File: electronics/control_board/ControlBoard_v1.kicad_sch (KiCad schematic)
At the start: 27 parts, among them J1 Motor1, J2 Motor2, J3 Motor3, J4 Encoder, J5 I2C, J7 Power, U1 ROB-14450, U2 ROB-14450, U3 ROB-14450, U4 DCDC_Converter

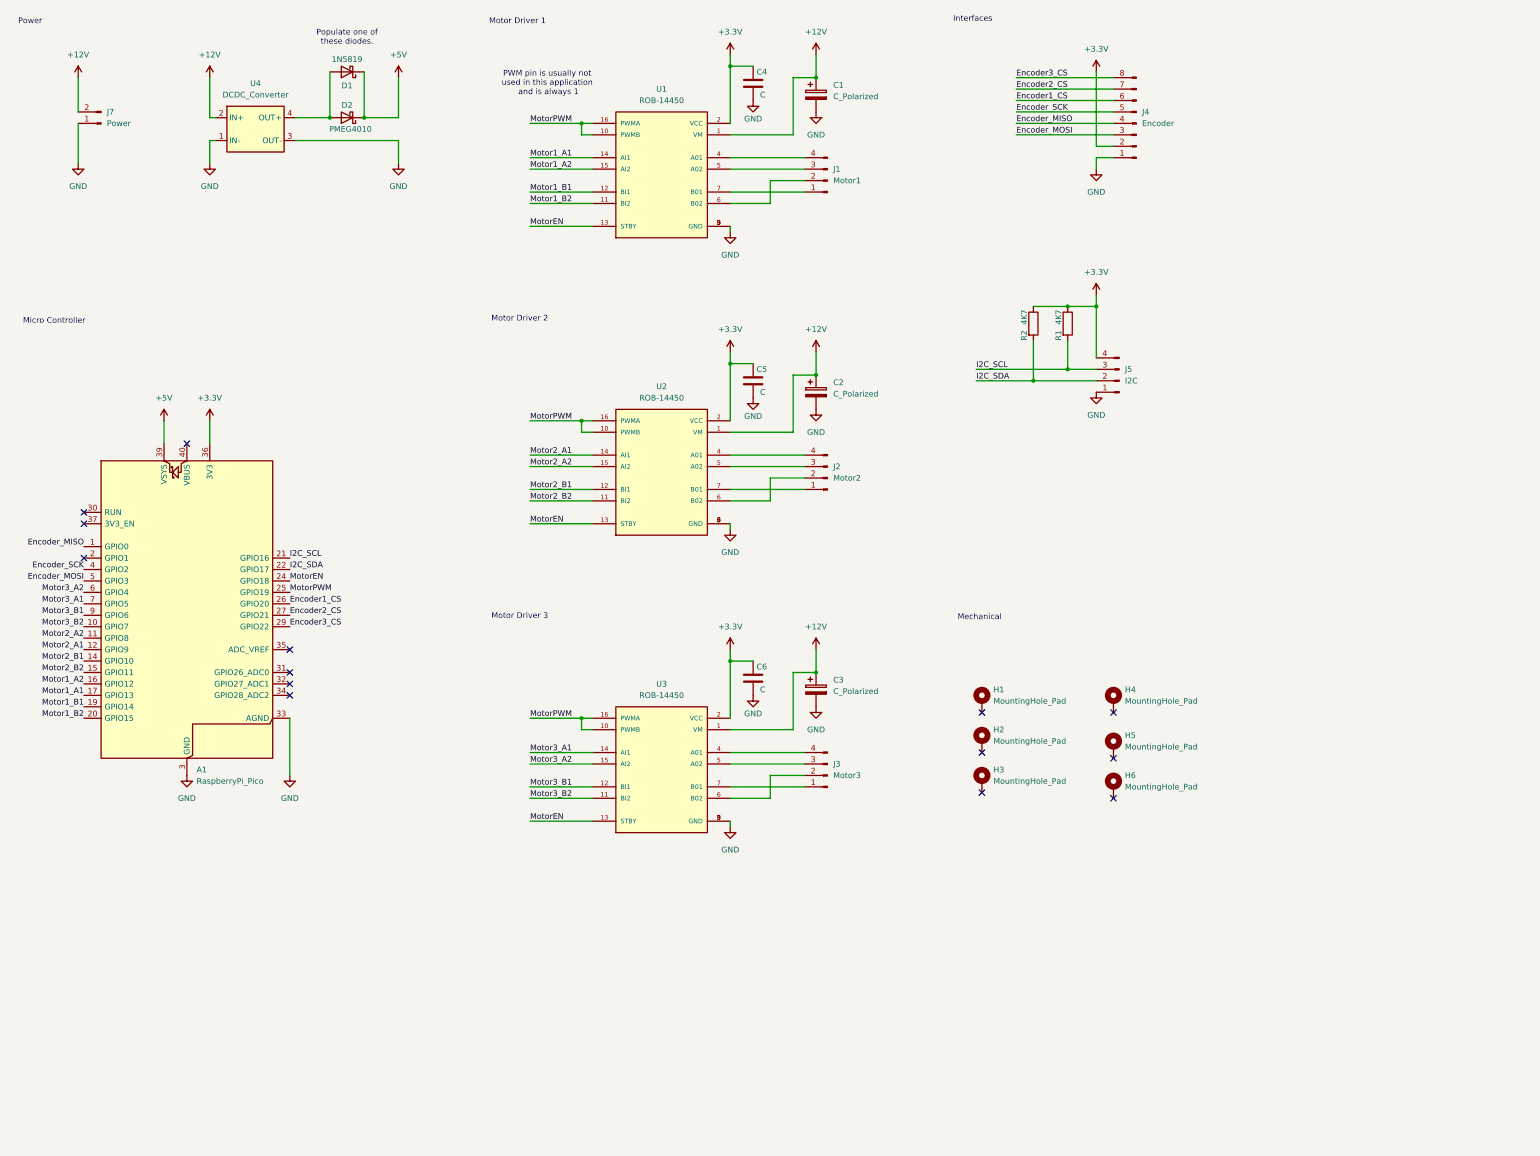
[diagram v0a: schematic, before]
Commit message: Worked on PCB (moved to 4 layers)
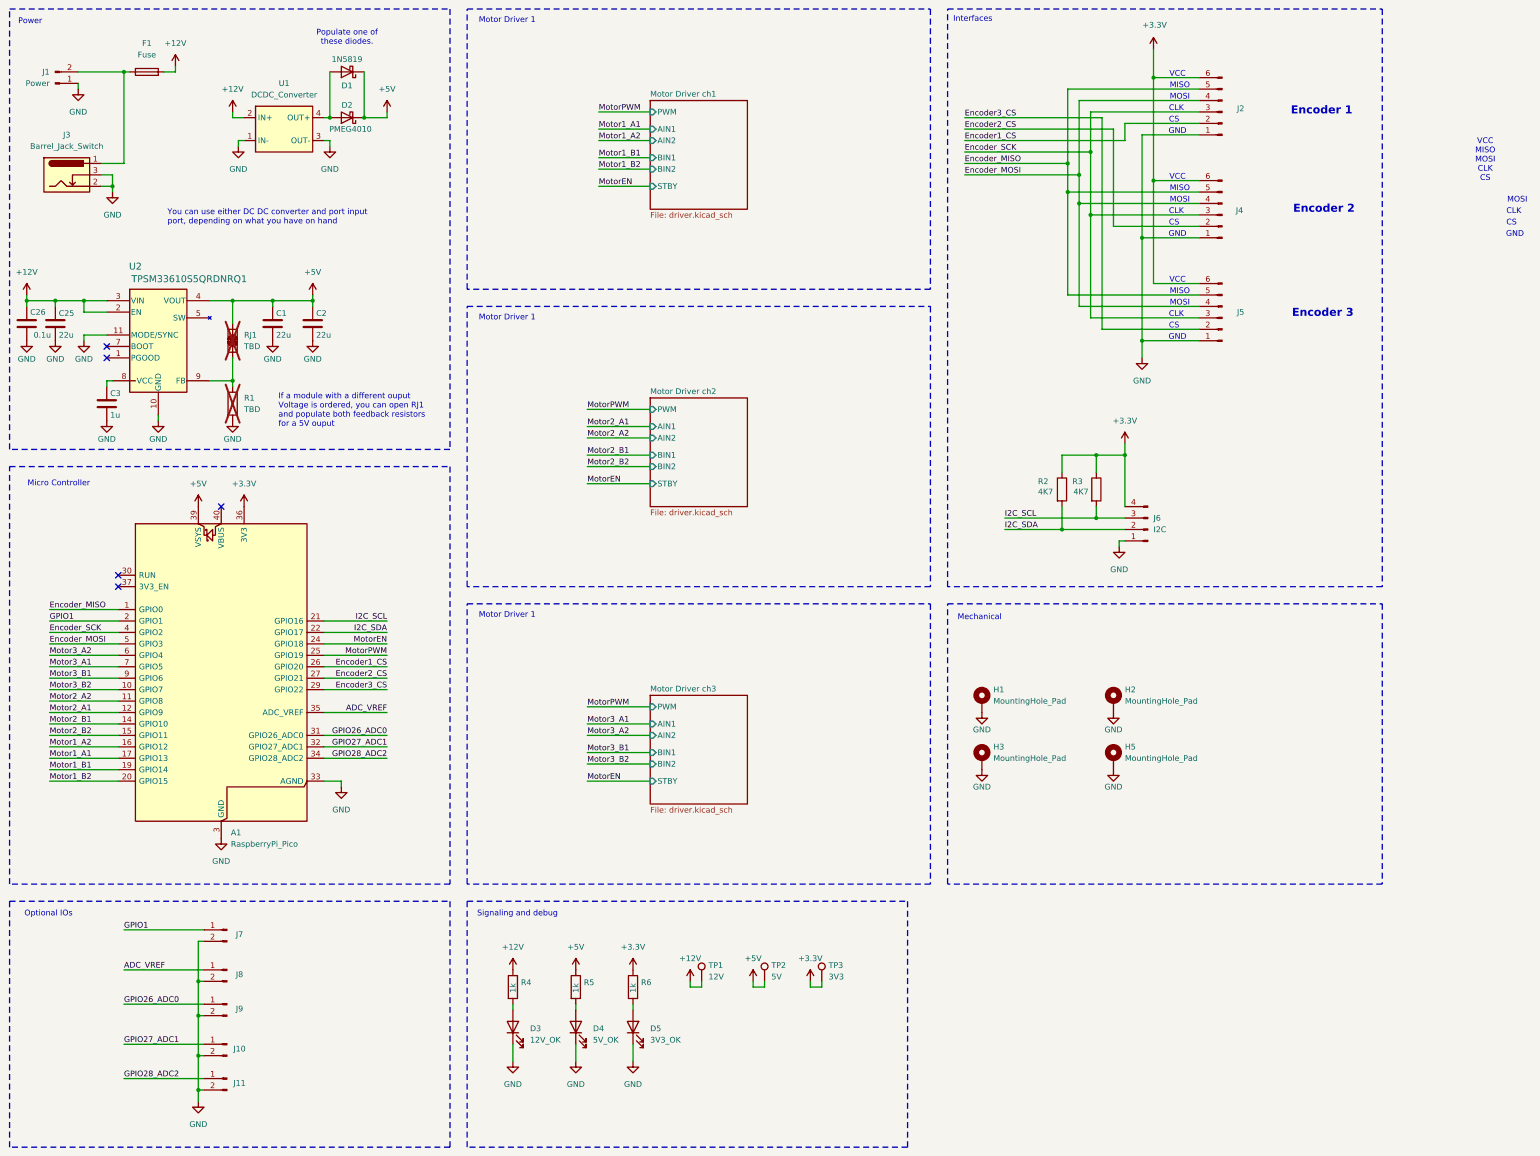
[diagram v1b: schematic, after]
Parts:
- removed C1, C2, C3: C_Polarized, Capacitor_THT:CP_Radial_D8.0mm_P3.50mm, symbol Device:C_Polarized
- removed C4, C5, C6: C, Capacitor_SMD:C_0603_1608Metric_Pad1.08x0.95mm_HandSolder, symbol Device:C
- removed H5, H6: MountingHole_Pad, MountingHole:MountingHole_2.7mm_M2.5_Pad_Via, symbol Mechanical:MountingHole_Pad
- removed J1: Motor1, Connector_PinHeader_2.54mm:PinHeader_1x04_P2.54mm_Vertical, symbol Connector:Conn_01x04_Pin
- removed J2: Motor2, Connector_PinHeader_2.54mm:PinHeader_1x04_P2.54mm_Vertical, symbol Connector:Conn_01x04_Pin
- removed J3: Motor3, Connector_PinHeader_2.54mm:PinHeader_1x04_P2.54mm_Vertical, symbol Connector:Conn_01x04_Pin
- removed J4: Encoder, Connector_JST:JST_PH_B8B-PH-K_1x08_P2.00mm_Vertical, symbol Connector:Conn_01x08_Pin
- removed U1, U2, U3: ROB-14450, ROB-14450:MODULE_ROB-14450, symbol ROB-14450:ROB-14450
- added C1, C2, C25: 22u, Capacitor_SMD:C_0805_2012Metric_Pad1.18x1.45mm_HandSolder, symbol Device:C
- added C26: 0.1u, Capacitor_SMD:C_0603_1608Metric_Pad1.08x0.95mm_HandSolder, symbol Device:C
- added C3: 1u, Capacitor_SMD:C_0805_2012Metric_Pad1.18x1.45mm_HandSolder, symbol Device:C
- added D3: 12V_OK, LED_SMD:LED_0805_2012Metric_Pad1.15x1.40mm_HandSolder, symbol Device:LED
- added D4: 5V_OK, LED_SMD:LED_0805_2012Metric_Pad1.15x1.40mm_HandSolder, symbol Device:LED
- added D5: 3V3_OK, LED_SMD:LED_0805_2012Metric_Pad1.15x1.40mm_HandSolder, symbol Device:LED
- added F1: Fuse, Fuse:Fuse_1206_3216Metric_Pad1.42x1.75mm_HandSolder, symbol Device:Fuse
- added J10, J11, J7, J8, J9: Conn_01x02_Pin, Connector_PinHeader_2.54mm:PinHeader_1x02_P2.54mm_Vertical, symbol Connector:Conn_01x02_Pin
- added J2, J4, J5: Conn_01x06_Pin, Connector_JST:JST_PH_B6B-PH-K_1x06_P2.00mm_Vertical, symbol Connector:Conn_01x06_Pin
- added J3: Barrel_Jack_Switch, Connector_BarrelJack:BarrelJack_Horizontal, symbol Connector:Barrel_Jack_Switch
- added R1: TBD, Resistor_SMD:R_0603_1608Metric_Pad0.98x0.95mm_HandSolder, symbol Device:R
- added R4, R5, R6: 1k, Resistor_SMD:R_0603_1608Metric_Pad0.98x0.95mm_HandSolder, symbol Device:R
- added RJ1: TBD, Additions:0603_shorted_resistor, symbol additions:R_Optional
- added TP1: 12V, TestPoint:TestPoint_Pad_D2.0mm, symbol Connector:TestPoint
- added TP2: 5V, TestPoint:TestPoint_Pad_D2.0mm, symbol Connector:TestPoint
- added TP3: 3V3, TestPoint:TestPoint_Pad_D2.0mm, symbol Connector:TestPoint
- added U2: TPSM33610S5QRDNRQ1, Additions:TPSM33610S5QRDNRQ1, symbol additions:TPSM33610S3QRDNRQ1
- A1: Distributor (none) -> Digikey; Distributor Number (none) -> 2648-SC0918CT-ND
- D1: Distributor (none) -> Digikey; Distributor Number (none) -> 1801-1N5819CT-ND
- D2: Distributor (none) -> Digikey; Distributor Number (none) -> -
- H1: Distributor (none) -> -; Distributor Number (none) -> -
- H2: renamed from H4; Distributor (none) -> -; Distributor Number (none) -> -
- H3: renamed from H2; Distributor (none) -> -; Distributor Number (none) -> -
- H5: renamed from H3; Distributor (none) -> -; Distributor Number (none) -> -
- J1: renamed from J7; Distributor (none) -> Digikey; Distributor Number (none) -> 1738-1437-ND
- J6: renamed from J5; Distributor (none) -> Digikey; Distributor Number (none) -> 455-B4B-XH-A-ND
- R2: Distributor (none) -> Digikey; Distributor Number (none) -> 541-4.70KHCT-ND
- R3: renamed from R1; Distributor (none) -> Digikey; Distributor Number (none) -> 541-4.70KHCT-ND
- U1: renamed from U4; Distributor (none) -> ?; Distributor Number (none) -> -
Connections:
- net +12V: now also C25.1, C26.1, F1.2, R4.1, TP1.1, U2.2 (EN), U2.3 (VIN); no longer J1.2 (Pin_2)
- net +3.3V: now also J2.6 (Pin_6), J4.6 (Pin_6), J5.6 (Pin_6), R6.1, TP3.1
- net +5V: now also C1.1, C2.1, R5.1, RJ1.1, TP2.1, U2.4 (VOUT)
- net Encoder1_CS: now also J2.2 (Pin_2)
- net Encoder2_CS: now also J4.2 (Pin_2)
- net Encoder3_CS: now also J5.2 (Pin_2)
- net Encoder_MISO: now also J2.5 (Pin_5), J4.5 (Pin_5), J5.5 (Pin_5)
- net Encoder_MOSI: now also J2.4 (Pin_4), J4.4 (Pin_4), J5.4 (Pin_4)
- net Encoder_SCK: now also J2.3 (Pin_3), J4.3 (Pin_3), J5.3 (Pin_3)
- net GND: now also H1.1, H2.1, H3.1, H5.1, C1.2, C2.2, C25.2, C26.2, C3.2, D3.1 (K), D4.1 (K), D5.1 (K), J10.2 (Pin_2), J11.2 (Pin_2), J2.1 (Pin_1), J3.2, J3.3, J4.1 (Pin_1), J5.1 (Pin_1), J7.2 (Pin_2), J8.2 (Pin_2), J9.2 (Pin_2), R1.2, U2.10 (GND), U2.11 (MODE/SYNC)
- net GPIO1: now reaches A1.2 (GPIO1)
- net GPIO1: now also J7.1 (Pin_1)
- net GPIO26_ADC0: now reaches A1.31 (GPIO26_ADC0)
- net GPIO26_ADC0: now also J9.1 (Pin_1)
- net GPIO27_ADC1: now reaches A1.32 (GPIO27_ADC1)
- net GPIO27_ADC1: now also J10.1 (Pin_1)
- net GPIO28_ADC2: now reaches A1.34 (GPIO28_ADC2)
- net GPIO28_ADC2: now also J11.1 (Pin_1)
- net ADC_VREF: now reaches A1.35 (ADC_VREF)
- net ADC_VREF: now also J8.1 (Pin_1)
- new net: D5.2 (A), R6.2
- new net: R1.1, RJ1.2, U2.9 (FB)
- new net: F1.1, J1.2 (Pin_2), J3.1
- new net: C3.1, U2.8 (VCC)
- new net: D3.2 (A), R4.2
- new net: U2.5 (SW), U2.6 (SW)
- new net: D4.2 (A), R5.2
- no-connect marks 14 -> 5
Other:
- added sheet Motor Driver ch1 (driver.kicad_sch)
- added sheet Motor Driver ch2 (driver.kicad_sch)
- added sheet Motor Driver ch3 (driver.kicad_sch)
- note added: "CLK"
- note added: "CS"
- note added: "Encoder 1"
- note added: "Encoder 2"
- note added: "Encoder 3"
- note added: "GND"
- note added: "If a module with a different ouput Voltage is ordered, you can open RJ1 and populate both feedback resistors for a 5V ouput"
- note added: "MISO"
- note added: "MOSI"
- note added: "Optional IOs"
- note added: "Signaling and debug"
- note added: "VCC"
- note added: "VCC MISO MOSI CLK CS"
- note added: "You can use either DC DC converter and port input port, depending on what you have on hand"
- note removed: "Motor Driver 2"
- note removed: "Motor Driver 3"
- note removed: "PWM pin is usually not used in this application and is always 1"
- moved on the sheet: A1, H3, H5, J1, J6, R2, R3, U1

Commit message: Worked on schematic and layout Added logo
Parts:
- added R10, R4, R5, R6: 4K7, Resistor_SMD:R_0603_1608Metric_Pad0.98x0.95mm_HandSolder, symbol Device:R
- F1: value Fuse -> 7A
- R7: renamed from R4; value 1k -> 4k7
- renumbered C26 to C1, C25 to C2, C1 to C3, C2 to C4, C3 to C5, H5 to H4, R5 to R8, R6 to R9
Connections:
- net +3.3V: now also R4.1, R5.1, R6.1
- net Encoder1_CS: now also R6.2
- net Encoder2_CS: now also R5.2
- net Encoder3_CS: now also R4.2
- net GND: now also R10.2
- net I2C_SCL: now also A1.22 (GPIO17), R2.2; no longer A1.21 (GPIO16), R3.2
- net I2C_SDA: now also A1.21 (GPIO16), R3.2; no longer A1.22 (GPIO17), R2.2
- net MotorEN: now also R10.1
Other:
- note added: "<- sample values, adjust to used LED's"
- note added: "<-shorted if unpopulated"
- note added: "I2C"
- note added: "If a module with a different output Voltage is ordered, you can open RJ1 and populate both feedback resistors for a 5V output"
- note added: "Motor Driver 2"
- note added: "Motor Driver 3"
- note added: "Pull Up / Down Resistors"
- note added: "Signaling and Debug"
- note added: "You can use either DC DC converter and input port, depending on what you have on hand"
- note added: "optional (IC's have internal pulldowns)"
- note removed: "If a module with a different ouput Voltage is ordered, you can open RJ1 and populate both feedback resistors for a 5V ouput"
- note removed: "Signaling and debug"
- note removed: "VCC MISO MOSI CLK CS"
- note removed: "You can use either DC DC converter and port input port, depending on what you have on hand"
- title: (none) -> Main control section
- moved on the sheet: C3, C4, J10, J11, J7, J8, J9, TP1, TP2, TP3

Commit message: Worked on PCB and Schematic, created production files
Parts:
- added D3: SMAJ12CA, Diode_SMD:D_SMA_Handsoldering, symbol Device:D_TVS
- D4: renamed from D3; Distributor (none) -> ?; Distributor Number (none) -> -
- D5: renamed from D4; Distributor (none) -> ?; Distributor Number (none) -> -
- D6: renamed from D5; Distributor (none) -> ?; Distributor Number (none) -> -
- R10, R2, R3, R4, R5, R6: value 4K7 -> 4k7
- R7: Distributor (none) -> Digikey; Distributor Number (none) -> 541-4.70KHCT-ND
- R8, R9: Distributor (none) -> Digikey; Distributor Number (none) -> 541-1.00KHCT-ND
- TP1, TP2, TP3: Distributor (none) -> -; Distributor Number (none) -> -; now left out of the parts list
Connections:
- net +12V: now also D3.2 (A2)
- net GND: now also D3.1 (A1)
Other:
- note added: "keep encoders CS lines high before internal pullups can be configured"
- note added: "optional"
- moved on the sheet: F1

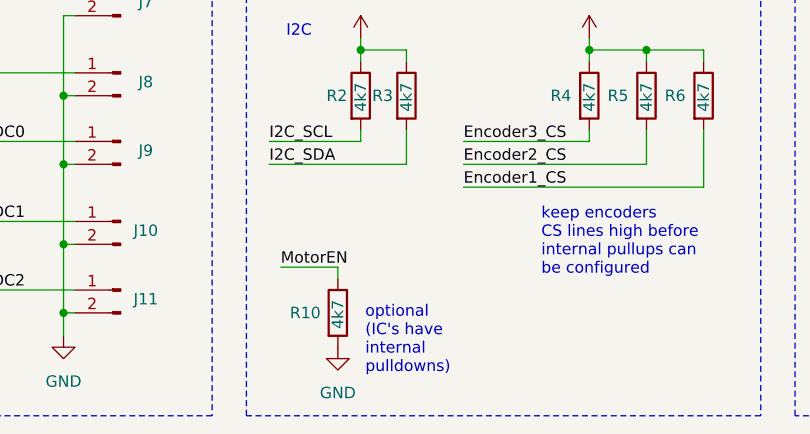
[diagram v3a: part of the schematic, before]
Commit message: Fixed wrong ordering numbers Regenerated IBOM with corrected settings to exclude TP's
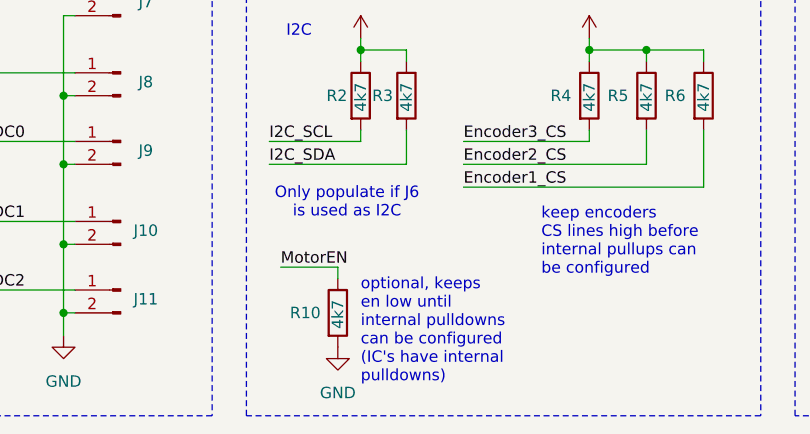
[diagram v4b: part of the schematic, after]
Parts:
- J2, J4, J5: Distributor Number 455-B6B-XH-A-ND -> 455-1708-ND
- J6: Distributor Number 455-B4B-XH-A-ND -> 455-1706-ND
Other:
- note added: "Only populate if J6 is used as I2C"
- note added: "optional, keeps en low until internal pulldowns can be configured (IC's have internal pulldowns)"
- note removed: "optional (IC's have internal pulldowns)"
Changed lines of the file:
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@@
 		)
 	)
+	(text "Only populate if J6\nis used as I2C"
+		(exclude_from_sim no)
+		(at 100.076 258.318 0)
+		(effects
+			(font
+				(size 1.27 1.27)
+			)
+		)
+	)
 	(text "Encoder 2"
 		(exclude_from_sim no)
@@
 		)
 	)
-	(text "optional\n(IC's have \ninternal\npulldowns)"
+	(text "optional, keeps\nen low until\ninternal pulldowns\ncan be configured\n(IC's have internal\npulldowns)"
 		(exclude_from_sim no)
-		(at 102.108 273.558 0)
+		(at 101.6 272.542 0)
 		(effects
 			(font
@@
 			)
 		)
-		(property "Distributor Number" "455-B6B-XH-A-ND"
+		(property "Distributor Number" "455-1708-ND"
 			(at 317.5 97.79 0)
 			(hide yes)
@@
 			)
 		)
-		(property "Distributor Number" "455-B6B-XH-A-ND"
+		(property "Distributor Number" "455-1708-ND"
 			(at 317.5 52.07 0)
 			(hide yes)
@@
 			)
 		)
-		(property "Distributor Number" "455-B4B-XH-A-ND"
+		(property "Distributor Number" "455-1706-ND"
 			(at 300.99 144.78 0)
 			(hide yes)
@@
 			)
 		)
-		(property "Distributor Number" "455-B6B-XH-A-ND"
+		(property "Distributor Number" "455-1708-ND"
 			(at 317.5 74.93 0)
 			(hide yes)
